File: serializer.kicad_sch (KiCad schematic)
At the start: 34 parts, among them U6 MAX9295A, Y1 Resonator_25MHz_ABM8G

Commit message: Improve layout
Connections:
- net VDDIO is gone; now on net +3V3: R18.2, R21.2
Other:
- moved on the sheet: R21, R22

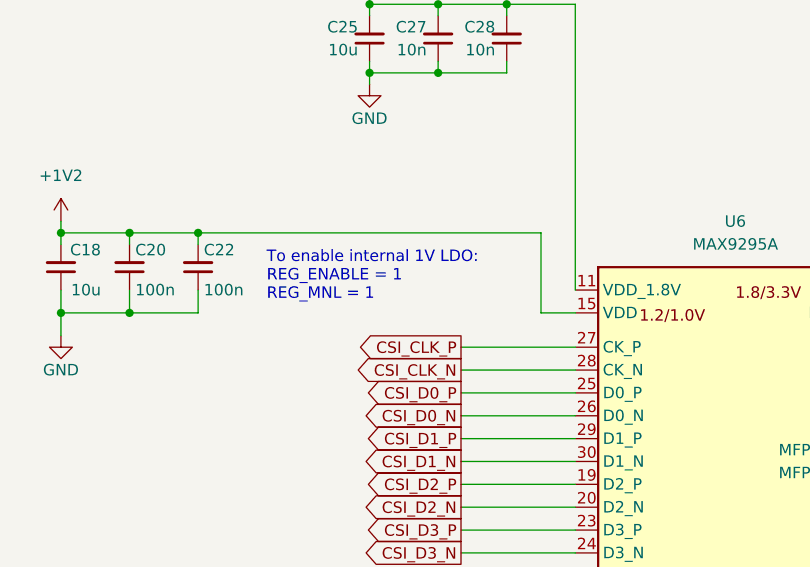
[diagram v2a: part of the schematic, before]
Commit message: [#53377] Add LDO config register addresses to schematic
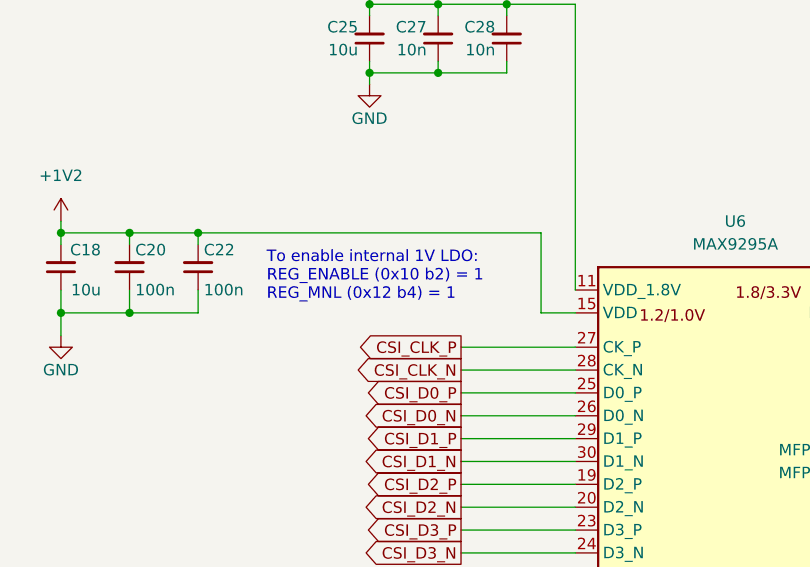
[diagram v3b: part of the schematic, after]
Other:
- note added: "To enable internal 1V LDO: REG_ENABLE (0x10 b2) = 1 REG_MNL (0x12 b4) = 1"
- note removed: "To enable internal 1V LDO: REG_ENABLE = 1 REG_MNL = 1"
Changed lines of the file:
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@@
     (effects (font (size 1.27 1.27)) (justify left bottom))
   )
-  (text "To enable internal 1V LDO:\nREG_ENABLE = 1 \nREG_MNL = 1"
+  (text "To enable internal 1V LDO:\nREG_ENABLE (0x10 b2) = 1 \nREG_MNL (0x12 b4) = 1"
     (at 124.46 94.615 0)
     (effects (font (size 1.27 1.27)) (justify left bottom))

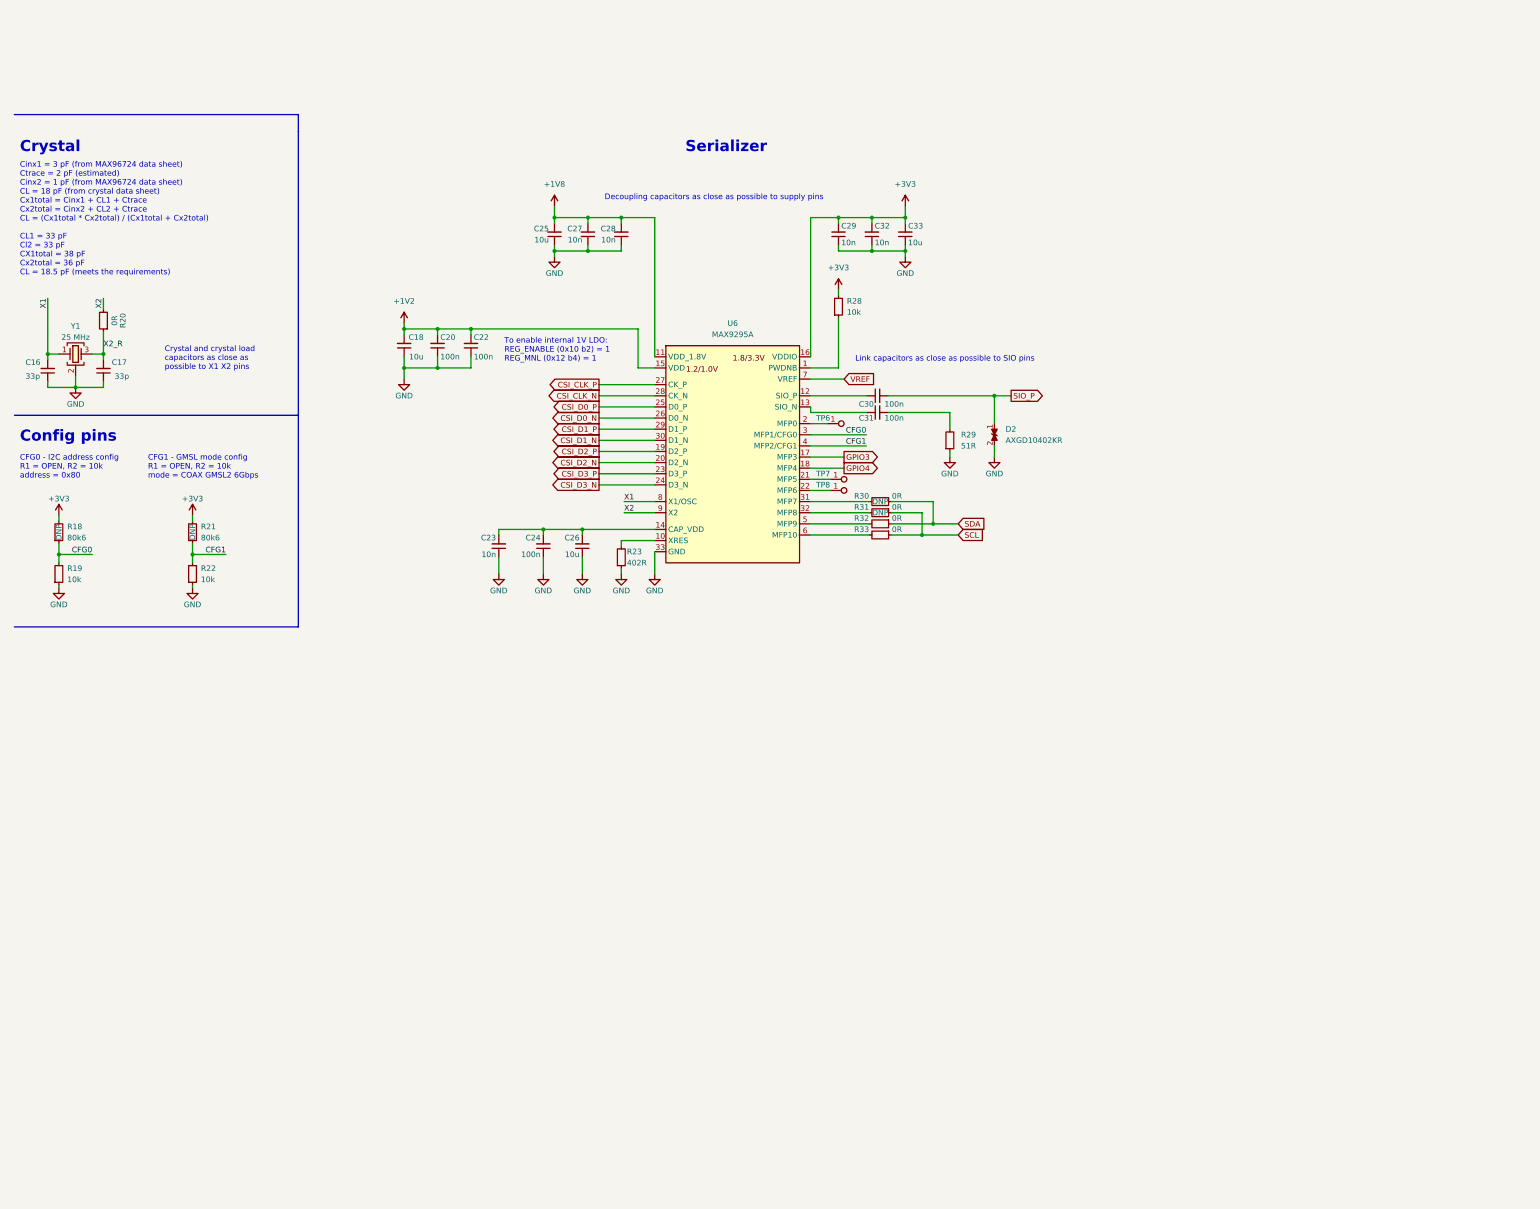
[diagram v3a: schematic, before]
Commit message: Update naming convention
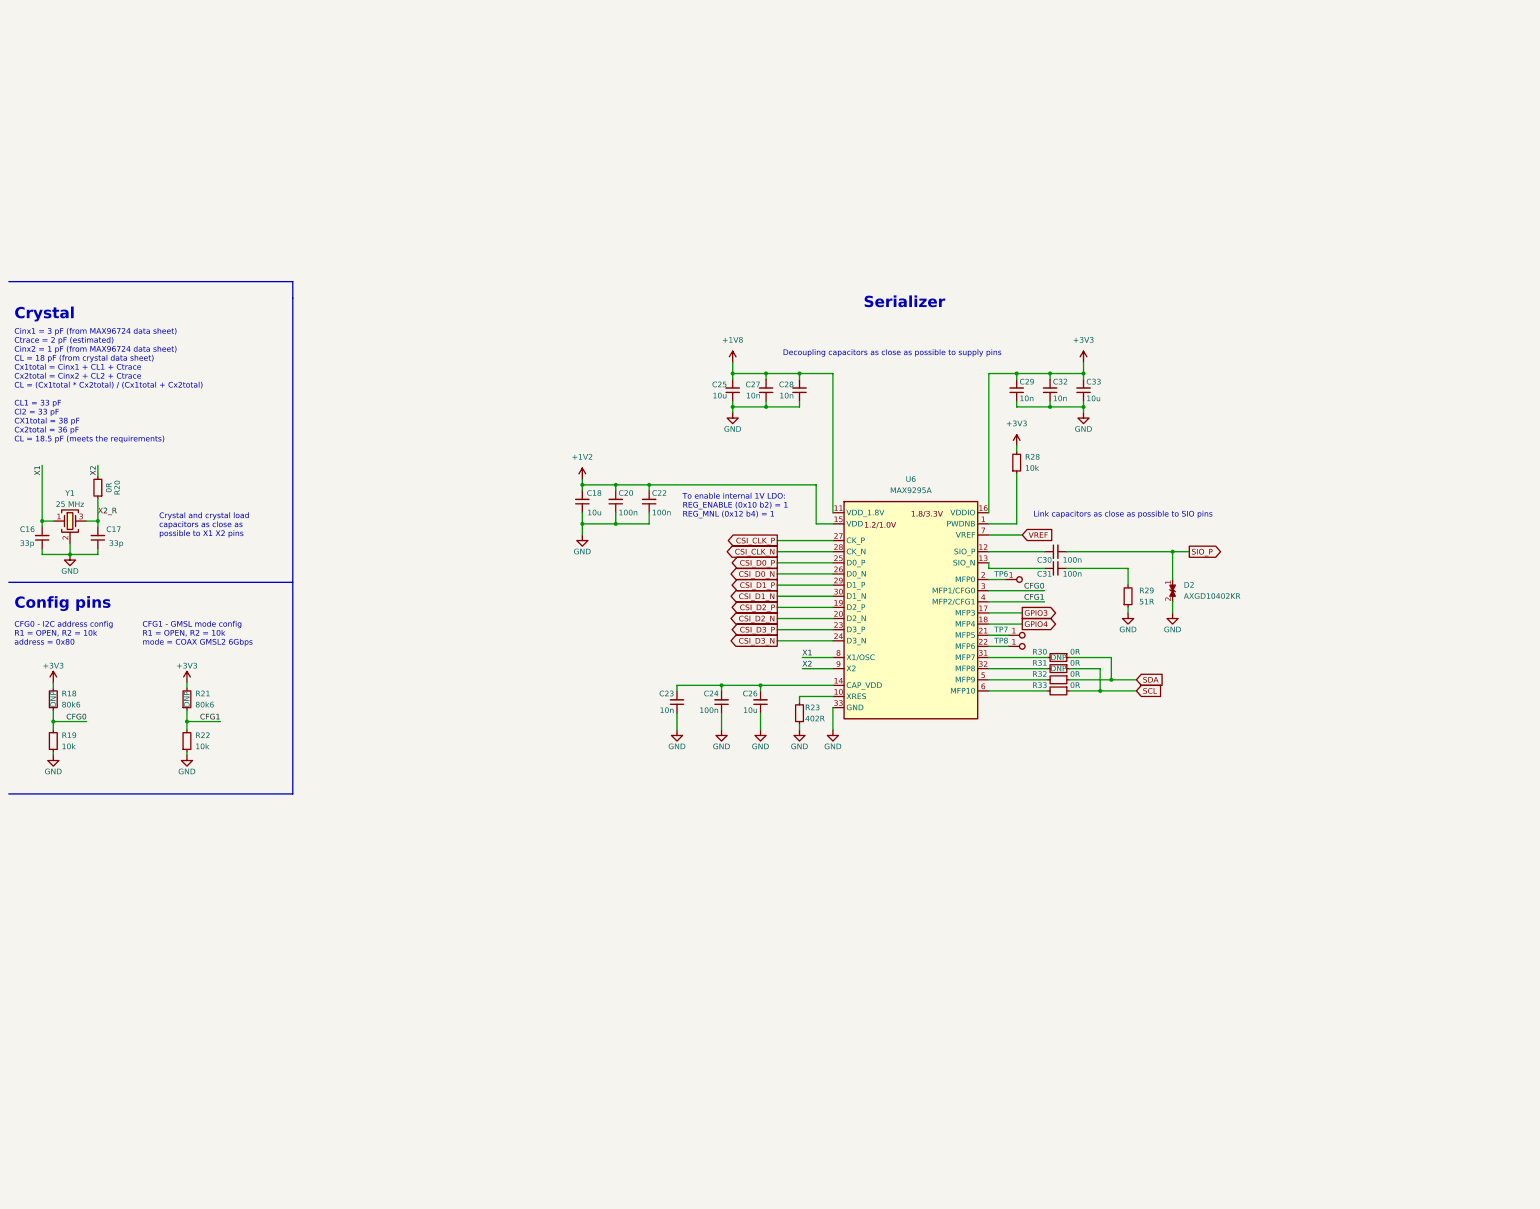
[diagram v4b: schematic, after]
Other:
- moved on the sheet: C16, C17, C18, C20, C22, C23, C24, C25, C26, C27, C28, C29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

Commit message: [#55438] Add LED indicators to schematics
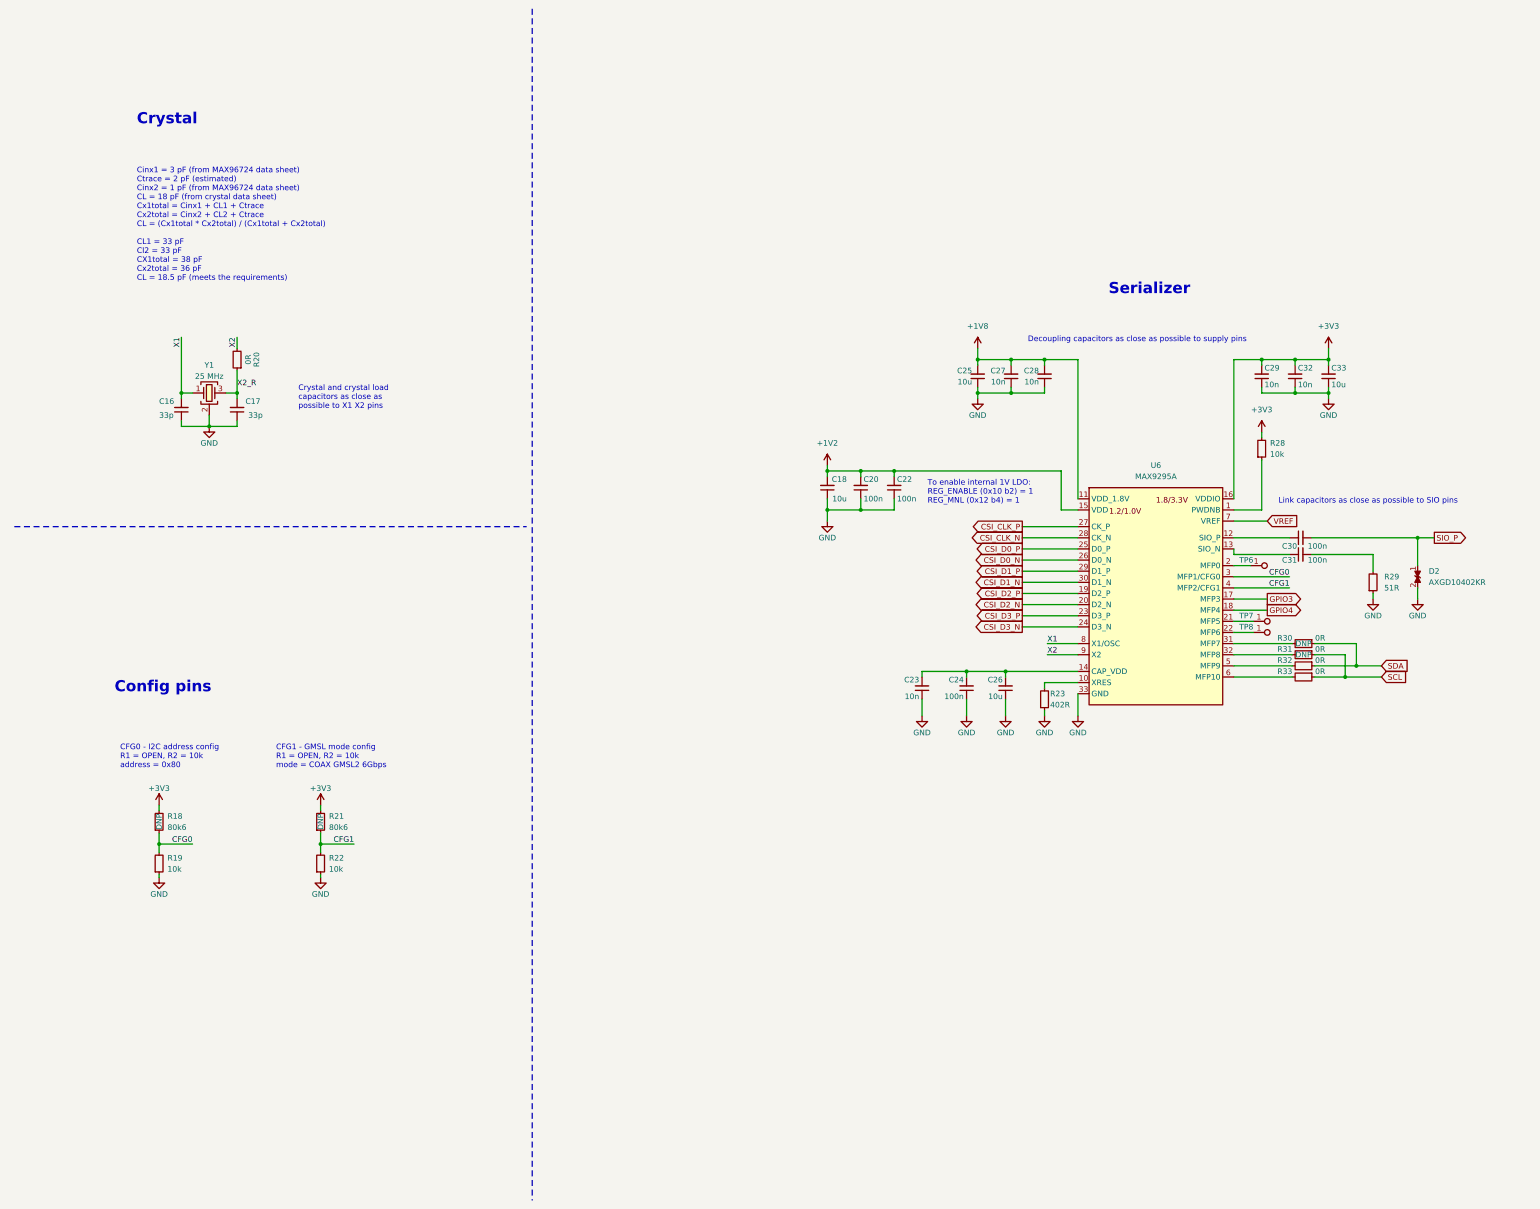
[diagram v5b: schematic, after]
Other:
- moved on the sheet: C16, C17, C18, C20, C22, C23, C24, C25, C26, C27, C28, C29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

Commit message: [#55438] Place LED indicators on PCB
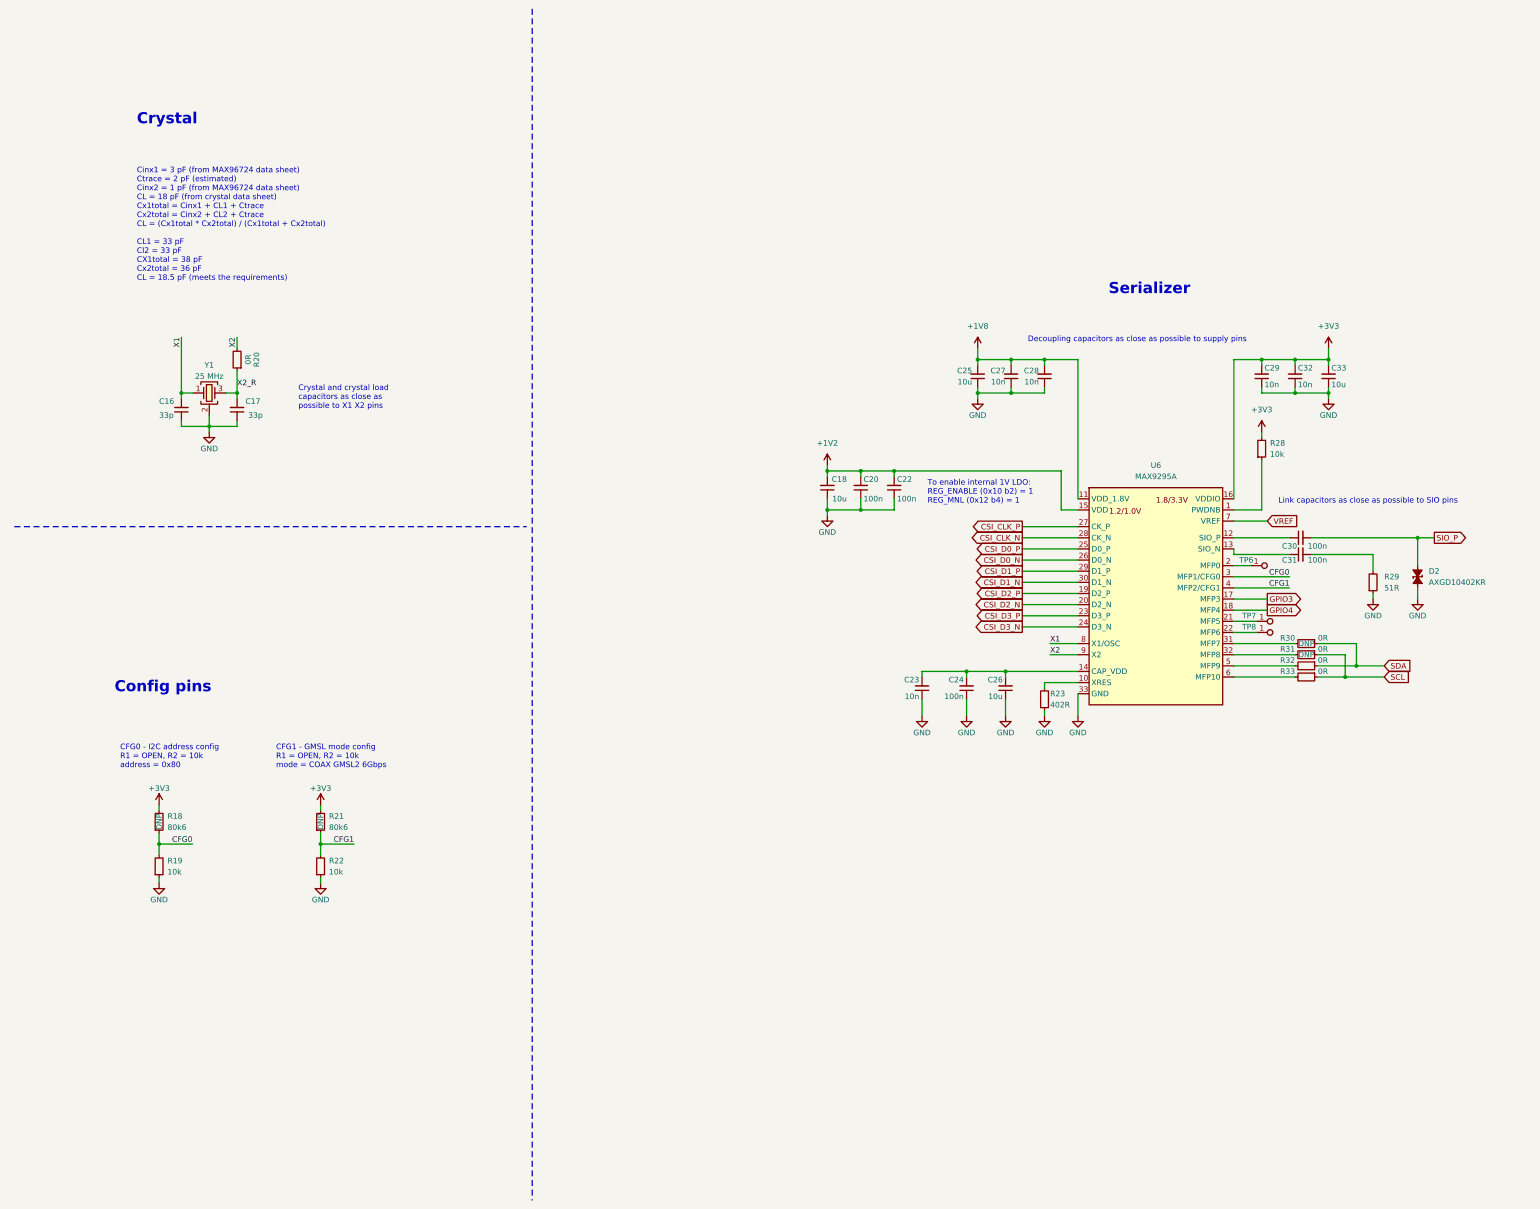
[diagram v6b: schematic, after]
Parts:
- R23: Manufacturer Vishay -> Bourns
- Y1: footprint antmicro-footprints:Oscillator_SMD_Geyer_KX-7-4Pin_3.2x2.5mm -> antmicro-footprints:Resonator_SMD_Abracon_ABM8G_3.2x2.5mm
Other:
- moved on the sheet: R19, R22, R30, R31, R32, R33, TP7, TP8

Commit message: [#55438] Update components
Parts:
- U6: Manufacturer Maxim Integrated Products -> Maxim Integrated
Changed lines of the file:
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@@
       (effects (font (size 1.27 1.27) (thickness 0.15)))
     )
-    (property "Manufacturer" "Maxim Integrated Products" (at 306.07 140.97 0)
+    (property "Manufacturer" "Maxim Integrated" (at 306.07 140.97 0)
       (effects (font (size 1.27 1.27) (thickness 0.15)) (justify left bottom) hide)
     )

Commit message: [#65118] Update assets
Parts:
- U6: Manufacturer Maxim Integrated -> Maxim Integrated Products
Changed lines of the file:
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@@
       (effects (font (size 1.27 1.27) (thickness 0.15)))
     )
-    (property "Manufacturer" "Maxim Integrated" (at 306.07 140.97 0)
+    (property "Manufacturer" "Maxim Integrated Products" (at 306.07 140.97 0)
       (effects (font (size 1.27 1.27) (thickness 0.15)) (justify left bottom) hide)
     )
